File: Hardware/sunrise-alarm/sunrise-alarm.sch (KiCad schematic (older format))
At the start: 15 parts

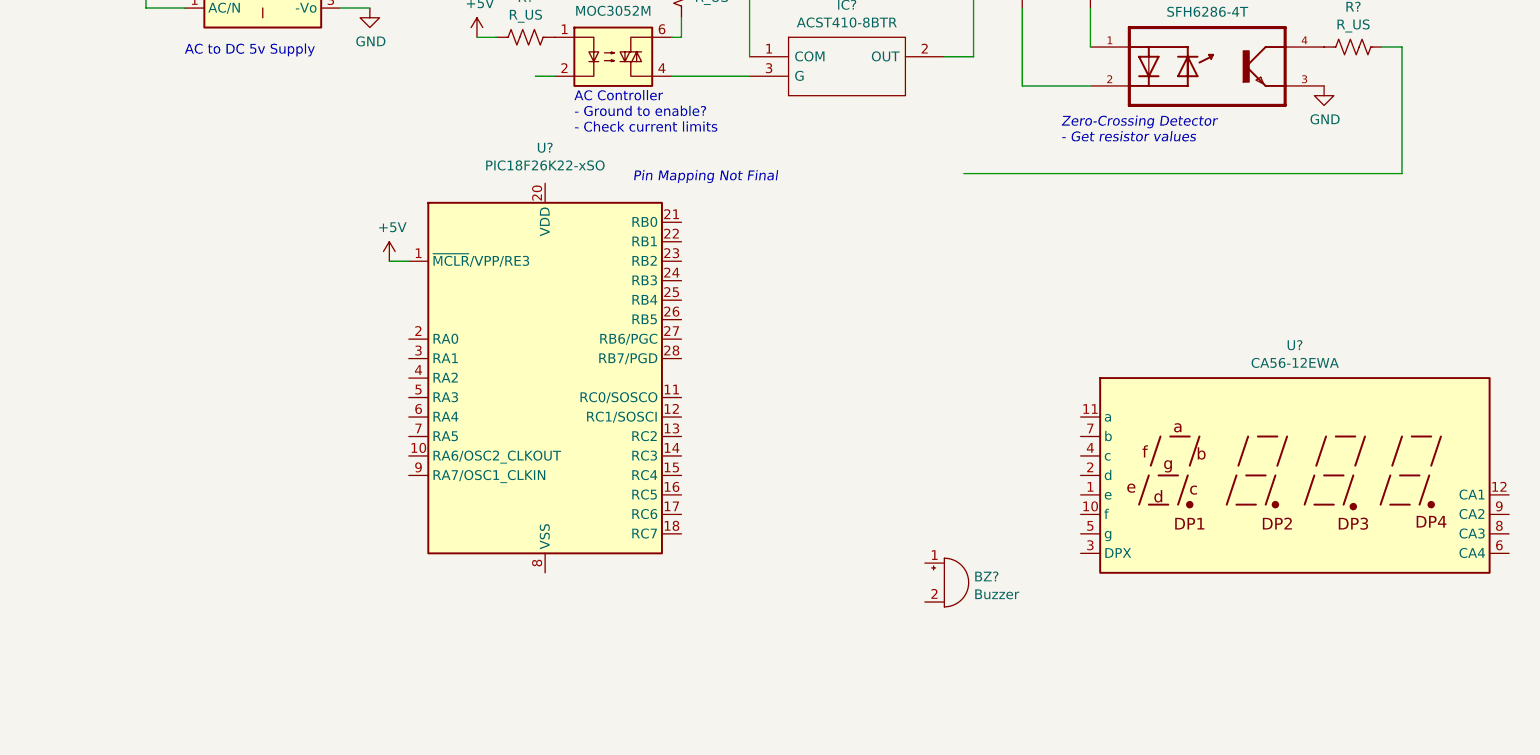
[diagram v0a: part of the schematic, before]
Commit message: Updated schematic, reset button, labeled lines
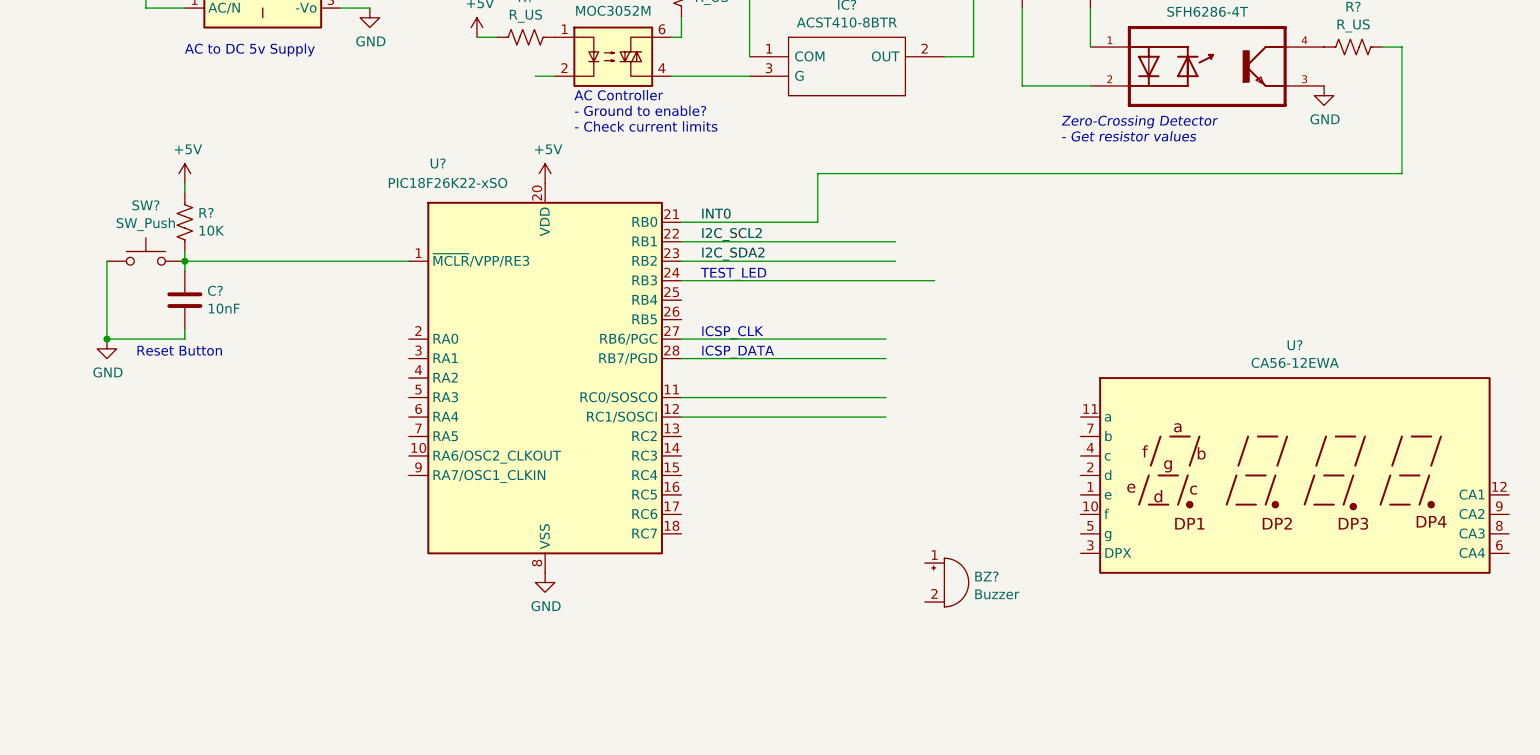
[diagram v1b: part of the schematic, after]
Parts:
- added C?: 10nF, symbol Device:C
- added R?: 10K, symbol Device:R_US
- added SW?: SW_Push, symbol Switch:SW_Push
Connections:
- net labels added: I2C_SCL2, I2C_SDA2, INT0
- wire segments 32 -> 47
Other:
- note added: "ICSP_CLK"
- note added: "ICSP_DATA"
- note added: "Reset Button"
- note added: "TEST_LED"
- note removed: "Pin Mapping Not Final"
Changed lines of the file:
@@
 $EndDescr
-$Comp
-L MCU_Microchip_PIC18:PIC18F26K22-xSO U?
-U 1 1 61792C0A
-P 3250 3450
-F 0 "U?" H 3250 4631 50  0000 C CNN
-F 1 "PIC18F26K22-xSO" H 3250 4540 50  0000 C CNN
-F 2 "Package_SO:SOIC-28W_7.5x17.9mm_P1.27mm" H 3450 3450 50  0001 C CNN
-F 3 "http://ww1.microchip.com/downloads/en/DeviceDoc/40001412G.pdf" H 3450 3450 50  0001 C CNN
-	1    3250 3450
-	1    0    0    -1
-$EndComp
 $Comp
 L Converter_ACDC:IRM-05-5 PS?
@@
 L power:+5V #PWR?
 U 1 1 617CDBCF
-P 2450 2850
-F 0 "#PWR?" H 2450 2700 50  0001 C CNN
-F 1 "+5V" H 2465 3023 50  0000 C CNN
-F 2 "" H 2450 2850 50  0001 C CNN
-F 3 "" H 2450 2850 50  0001 C CNN
-	1    2450 2850
-	1    0    0    -1
-$EndComp
-Wire Wire Line
-	2450 2850 2550 2850
+P 3250 2450
+F 0 "#PWR?" H 3250 2300 50  0001 C CNN
+F 1 "+5V" H 3265 2623 50  0000 C CNN
+F 2 "" H 3250 2450 50  0001 C CNN
+F 3 "" H 3250 2450 50  0001 C CNN
+	1    3250 2450
+	1    0    0    -1
+$EndComp
 Text Notes 8150 7650 0    50   ~ 0
 2021-10-27
@@
 Text Notes 5900 2250 0    50   Italic 0
 Zero-Crossing Detector\n- Get resistor values
-Text Notes 3700 2450 0    50   Italic 0
-Pin Mapping Not Final
 $Comp
 L Device:R_US R?
@@
 Wire Wire Line
 	7650 1750 7650 2400
-Wire Wire Line
-	7650 2400 5400 2400
+$Comp
+L power:GND #PWR?
+U 1 1 617BCF12
+P 3250 4450
+F 0 "#PWR?" H 3250 4200 50  0001 C CNN
+F 1 "GND" H 3255 4277 50  0000 C CNN
+F 2 "" H 3250 4450 50  0001 C CNN
+F 3 "" H 3250 4450 50  0001 C CNN
+	1    3250 4450
+	1    0    0    -1
+$EndComp
+Wire Wire Line
+	1400 2850 1400 2800
+$Comp
+L Device:R_US R?
+U 1 1 617BE3B8
+P 1400 2650
+F 0 "R?" H 1468 2696 50  0000 L CNN
+F 1 "10K" H 1468 2605 50  0000 L CNN
+F 2 "" V 1440 2640 50  0001 C CNN
+F 3 "~" H 1400 2650 50  0001 C CNN
+	1    1400 2650
+	1    0    0    -1
+$EndComp
+Wire Wire Line
+	1400 2500 1400 2450
+$Comp
+L power:+5V #PWR?
+U 1 1 617BF7D0
+P 1400 2450
+F 0 "#PWR?" H 1400 2300 50  0001 C CNN
+F 1 "+5V" H 1415 2623 50  0000 C CNN
+F 2 "" H 1400 2450 50  0001 C CNN
+F 3 "" H 1400 2450 50  0001 C CNN
+	1    1400 2450
+	1    0    0    -1
+$EndComp
+$Comp
+L Switch:SW_Push SW?
+U 1 1 617C3584
+P 1200 2850
+F 0 "SW?" H 1200 3135 50  0000 C CNN
+F 1 "SW_Push" H 1200 3044 50  0000 C CNN
+F 2 "" H 1200 3050 50  0001 C CNN
+F 3 "~" H 1200 3050 50  0001 C CNN
+	1    1200 2850
+	1    0    0    -1
+$EndComp
+Connection ~ 1400 2850
+$Comp
+L Device:C C?
+U 1 1 617C3D3F
+P 1400 3050
+F 0 "C?" H 1515 3096 50  0000 L CNN
+F 1 "10nF" H 1515 3005 50  0000 L CNN
+F 2 "" H 1438 2900 50  0001 C CNN
+F 3 "~" H 1400 3050 50  0001 C CNN
+	1    1400 3050
+	1    0    0    -1
+$EndComp
+Wire Wire Line
+	1400 3250 1000 3250
+Wire Wire Line
+	1000 3250 1000 2850
+$Comp
+L power:GND #PWR?
+U 1 1 617C5B85
+P 1000 3250
+F 0 "#PWR?" H 1000 3000 50  0001 C CNN
+F 1 "GND" H 1005 3077 50  0000 C CNN
+F 2 "" H 1000 3250 50  0001 C CNN
+F 3 "" H 1000 3250 50  0001 C CNN
+	1    1000 3250
+	1    0    0    -1
+$EndComp
+Connection ~ 1000 3250
+Wire Wire Line
+	1400 2900 1400 2850
+Wire Wire Line
+	1400 3250 1400 3200
+Wire Wire Line
+	1400 2850 2550 2850
+Text Notes 1150 3350 0    50   ~ 0
+Reset Button
+$Comp
+L MCU_Microchip_PIC18:PIC18F26K22-xSO U?
+U 1 1 61792C0A
+P 3250 3450
+F 0 "U?" H 2700 4550 50  0000 C CNN
+F 1 "PIC18F26K22-xSO" H 2750 4450 50  0000 C CNN
+F 2 "Package_SO:SOIC-28W_7.5x17.9mm_P1.27mm" H 3450 3450 50  0001 C CNN
+F 3 "http://ww1.microchip.com/downloads/en/DeviceDoc/40001412G.pdf" H 3450 3450 50  0001 C CNN
+	1    3250 3450
+	1    0    0    -1
+$EndComp
+Wire Wire Line
+	3950 2650 4650 2650
+Wire Wire Line
+	4650 2650 4650 2400
+Wire Wire Line
+	4650 2400 7650 2400
+Wire Wire Line
+	3950 2750 5050 2750
+Wire Wire Line
+	3950 2850 5050 2850
+Text Label 4050 2750 0    50   ~ 0
+I2C_SCL2
+Text Label 4050 2850 0    50   ~ 0
+I2C_SDA2
+Text Label 4050 2650 0    50   ~ 0
+INT0
+Wire Wire Line
+	3950 3550 5000 3550
+Wire Wire Line
+	3950 3650 5000 3650
+Wire Wire Line
+	3950 3250 5000 3250
+Wire Wire Line
+	3950 3350 5000 3350
+Text Notes 4050 3350 0    50   ~ 0
+ICSP_DATA
+Text Notes 4050 3250 0    50   ~ 0
+ICSP_CLK
+Text Notes 4050 2950 0    50   ~ 0
+TEST_LED
+Wire Wire Line
+	3950 2950 5250 2950
 $EndSCHEMATC

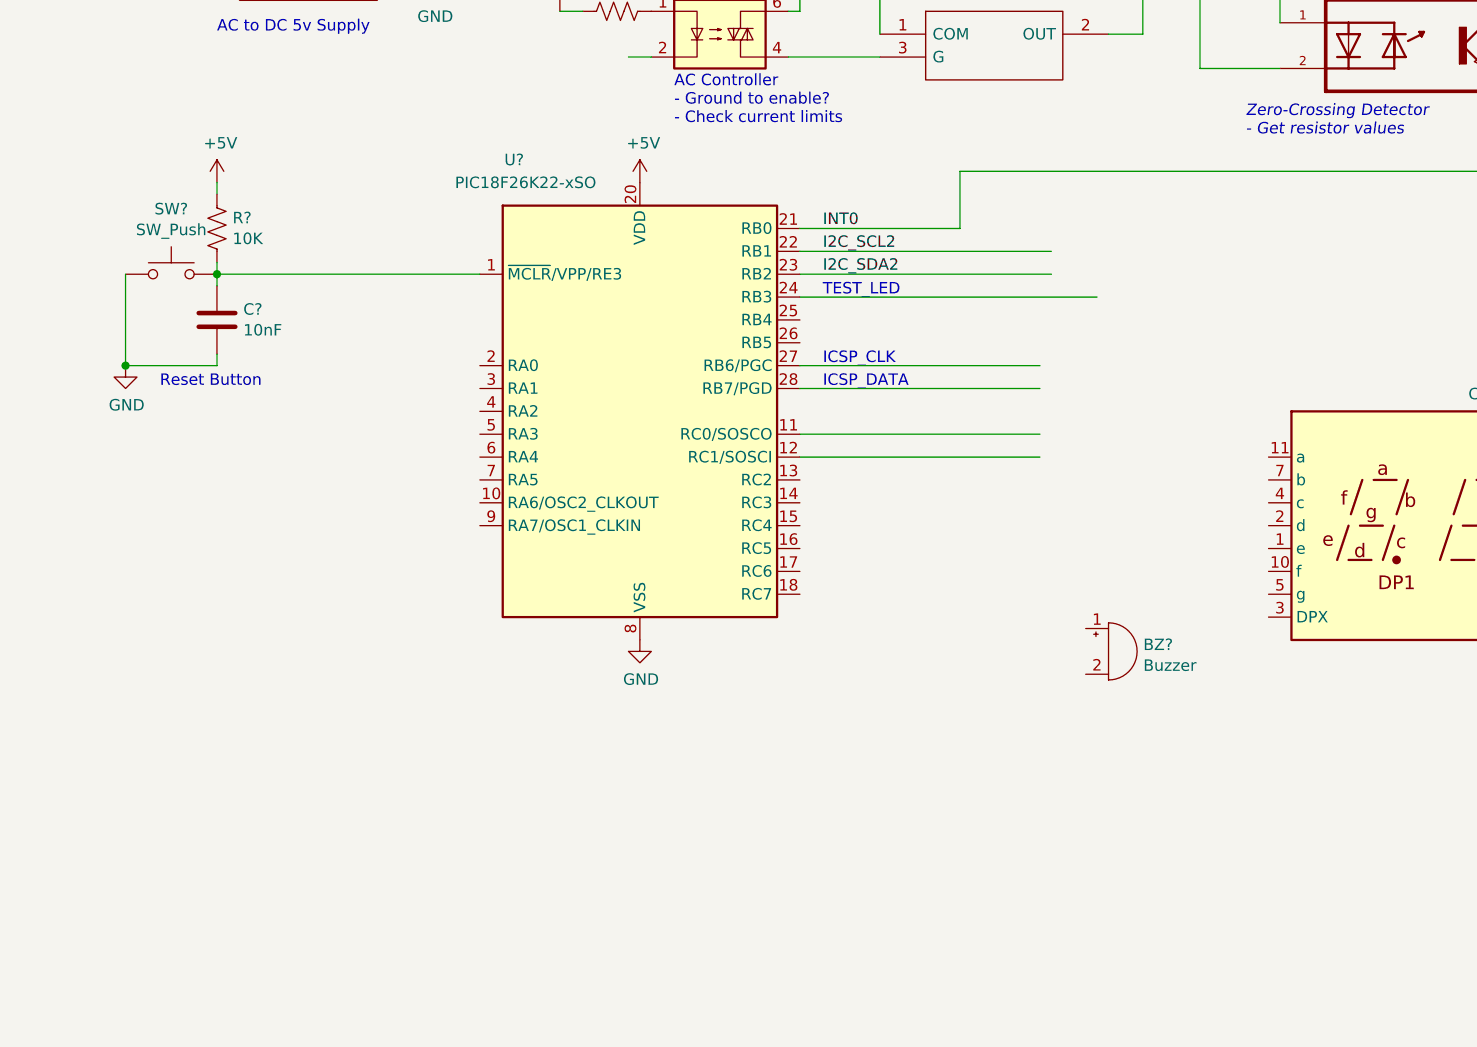
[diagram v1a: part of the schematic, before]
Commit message: Schematic: Added programing header
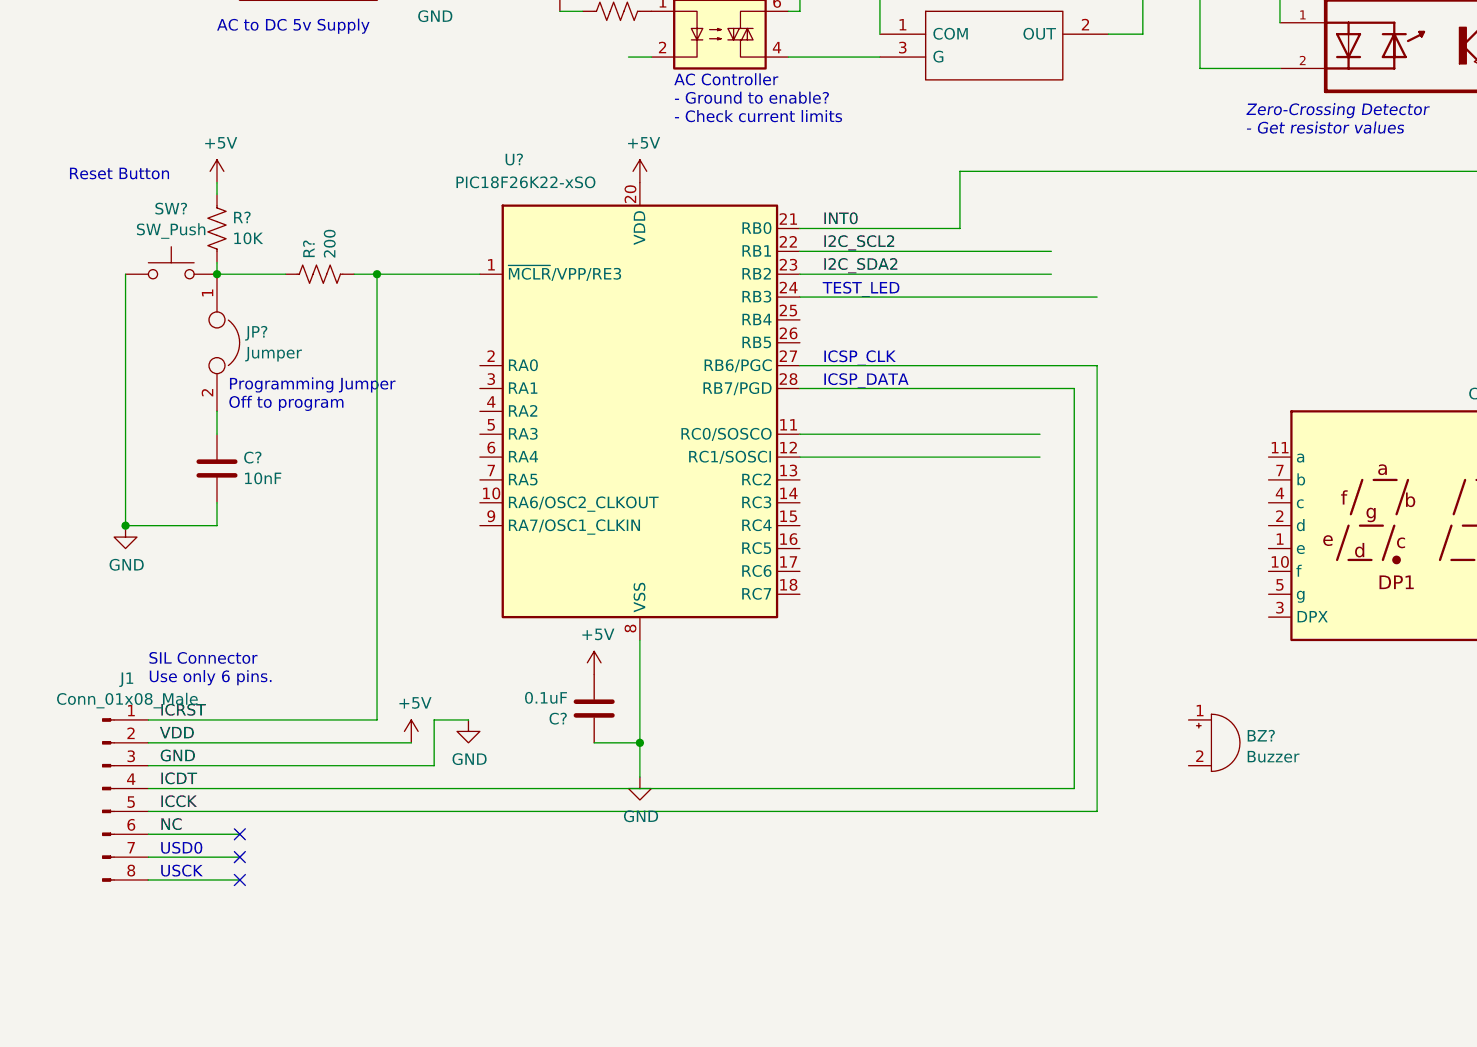
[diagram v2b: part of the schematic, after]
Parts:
- added C?: 0.1uF, symbol Device:C
- added J1: Conn_01x08_Male, symbol Connector:Conn_01x08_Male
- added JP?: Jumper, symbol Device:Jumper
- added R?: 200, symbol Device:R_US
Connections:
- net labels added: ICCK, ICDT, ICRST, NC, VDD
- wire segments 47 -> 65
- no-connect marks 0 -> 3
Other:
- note added: "Programming Jumper\nOff to program"
- note added: "SIL Connector\nUse only 6 pins."
- note added: "USCK"
- note added: "USD0"
- moved on the sheet: BZ?, C?
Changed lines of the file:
@@
 L Device:Buzzer BZ?
 U 1 1 617BFC39
-P 5300 4500
-F 0 "BZ?" H 5452 4529 50  0000 L CNN
-F 1 "Buzzer" H 5452 4438 50  0000 L CNN
-F 2 "" V 5275 4600 50  0001 C CNN
-F 3 "~" V 5275 4600 50  0001 C CNN
-	1    5300 4500
+P 5750 4900
+F 0 "BZ?" H 5902 4929 50  0000 L CNN
+F 1 "Buzzer" H 5902 4838 50  0000 L CNN
+F 2 "" V 5725 5000 50  0001 C CNN
+F 3 "~" V 5725 5000 50  0001 C CNN
+	1    5750 4900
 	1    0    0    -1
 $EndComp
@@
 Wire Wire Line
 	7650 1750 7650 2400
-$Comp
-L power:GND #PWR?
-U 1 1 617BCF12
-P 3250 4450
-F 0 "#PWR?" H 3250 4200 50  0001 C CNN
-F 1 "GND" H 3255 4277 50  0000 C CNN
-F 2 "" H 3250 4450 50  0001 C CNN
-F 3 "" H 3250 4450 50  0001 C CNN
-	1    3250 4450
-	1    0    0    -1
-$EndComp
 Wire Wire Line
 	1400 2850 1400 2800
@@
 L Device:C C?
 U 1 1 617C3D3F
-P 1400 3050
-F 0 "C?" H 1515 3096 50  0000 L CNN
-F 1 "10nF" H 1515 3005 50  0000 L CNN
-F 2 "" H 1438 2900 50  0001 C CNN
-F 3 "~" H 1400 3050 50  0001 C CNN
-	1    1400 3050
-	1    0    0    -1
-$EndComp
-Wire Wire Line
-	1400 3250 1000 3250
-Wire Wire Line
-	1000 3250 1000 2850
+P 1400 3700
+F 0 "C?" H 1515 3746 50  0000 L CNN
+F 1 "10nF" H 1515 3655 50  0000 L CNN
+F 2 "" H 1438 3550 50  0001 C CNN
+F 3 "~" H 1400 3700 50  0001 C CNN
+	1    1400 3700
+	1    0    0    -1
+$EndComp
+Wire Wire Line
+	1400 3950 1000 3950
 $Comp
 L power:GND #PWR?
 U 1 1 617C5B85
-P 1000 3250
-F 0 "#PWR?" H 1000 3000 50  0001 C CNN
-F 1 "GND" H 1005 3077 50  0000 C CNN
-F 2 "" H 1000 3250 50  0001 C CNN
-F 3 "" H 1000 3250 50  0001 C CNN
-	1    1000 3250
-	1    0    0    -1
-$EndComp
-Connection ~ 1000 3250
-Wire Wire Line
-	1400 2900 1400 2850
-Wire Wire Line
-	1400 3250 1400 3200
-Wire Wire Line
-	1400 2850 2550 2850
-Text Notes 1150 3350 0    50   ~ 0
+P 1000 3950
+F 0 "#PWR?" H 1000 3700 50  0001 C CNN
+F 1 "GND" H 1005 3777 50  0000 C CNN
+F 2 "" H 1000 3950 50  0001 C CNN
+F 3 "" H 1000 3950 50  0001 C CNN
+	1    1000 3950
+	1    0    0    -1
+$EndComp
+Connection ~ 1000 3950
+Wire Wire Line
+	1400 3950 1400 3850
+Wire Wire Line
+	1400 2850 1700 2850
+Text Notes 750  2450 0    50   ~ 0
 Reset Button
 $Comp
@@
 Wire Wire Line
 	3950 3650 5000 3650
-Wire Wire Line
-	3950 3250 5000 3250
-Wire Wire Line
-	3950 3350 5000 3350
 Text Notes 4050 3350 0    50   ~ 0
 ICSP_DATA
@@
 Wire Wire Line
 	3950 2950 5250 2950
+Wire Wire Line
+	1100 5300 1500 5300
+$Comp
+L Connector:Conn_01x08_Male J1
+U 1 1 61834A34
+P 900 5100
+F 0 "J1" H 1008 5581 50  0000 C CNN
+F 1 "Conn_01x08_Male" H 1008 5490 50  0000 C CNN
+F 2 "" H 900 5100 50  0001 C CNN
+F 3 "~" H 900 5100 50  0001 C CNN
+	1    900  5100
+	1    0    0    -1
+$EndComp
+$Comp
+L Device:C C?
+U 1 1 61839E19
+P 3050 4750
+F 0 "C?" H 3165 4796 50  0000 L CNN
+F 1 "0.1uF" H 3165 4705 50  0000 L CNN
+F 2 "" H 3088 4600 50  0001 C CNN
+F 3 "~" H 3050 4750 50  0001 C CNN
+	1    3050 4750
+	-1   0    0    1
+$EndComp
+$Comp
+L power:+5V #PWR?
+U 1 1 61845E96
+P 3050 4600
+F 0 "#PWR?" H 3050 4450 50  0001 C CNN
+F 1 "+5V" H 3065 4773 50  0000 C CNN
+F 2 "" H 3050 4600 50  0001 C CNN
+F 3 "" H 3050 4600 50  0001 C CNN
+	1    3050 4600
+	1    0    0    -1
+$EndComp
+$Comp
+L power:GND #PWR?
+U 1 1 61846300
+P 3250 5050
+F 0 "#PWR?" H 3250 4800 50  0001 C CNN
+F 1 "GND" H 3255 4877 50  0000 C CNN
+F 2 "" H 3250 5050 50  0001 C CNN
+F 3 "" H 3250 5050 50  0001 C CNN
+	1    3250 5050
+	1    0    0    -1
+$EndComp
+Wire Wire Line
+	3050 4900 3250 4900
+Wire Wire Line
+	3250 4900 3250 4450
+Connection ~ 3250 4900
+Wire Wire Line
+	3250 5050 3250 4900
+$Comp
+L Device:Jumper JP?
+U 1 1 6185279F
+P 1400 3150
+F 0 "JP?" V 1354 3277 50  0000 L CNN
+F 1 "Jumper" V 1445 3277 50  0000 L CNN
+F 2 "" H 1400 3150 50  0001 C CNN
+F 3 "~" H 1400 3150 50  0001 C CNN
+	1    1400 3150
+	0    1    1    0
+$EndComp
+Wire Wire Line
+	1000 2850 1000 3950
+Wire Wire Line
+	1400 3450 1400 3550
+Text Notes 1450 3450 0    50   ~ 0
+Programming Jumper\nOff to program
+$Comp
+L Device:R_US R?
+U 1 1 6186145D
+P 1850 2850
+F 0 "R?" H 1918 2896 50  0000 L CNN
+F 1 "200" H 1918 2805 50  0000 L CNN
+F 2 "" V 1890 2840 50  0001 C CNN
+F 3 "~" H 1850 2850 50  0001 C CNN
+	1    1850 2850
+	0    -1   -1   0
+$EndComp
+Wire Wire Line
+	2000 2850 2100 2850
+Text Notes 1100 4650 0    50   ~ 0
+SIL Connector\nUse only 6 pins.
+Text Label 1150 4800 0    50   ~ 0
+ICRST
+Text Label 1150 4900 0    50   ~ 0
+VDD
+Text Label 1150 5000 0    50   ~ 0
+GND
+Text Label 1150 5100 0    50   ~ 0
+ICDT
+Text Label 1150 5200 0    50   ~ 0
+ICCK
+Text Label 1150 5300 0    50   ~ 0
+NC
+NoConn ~ 1500 5300
+Wire Wire Line
+	1100 5400 1500 5400
+Wire Wire Line
+	1100 5500 1500 5500
+NoConn ~ 1500 5400
+NoConn ~ 1500 5500
+Text Notes 1150 5400 0    50   ~ 0
+USD0
+Text Notes 1150 5500 0    50   ~ 0
+USCK
+Wire Wire Line
+	2100 2850 2100 4800
+Wire Wire Line
+	1100 4800 2100 4800
+Connection ~ 2100 2850
+Wire Wire Line
+	2100 2850 2550 2850
+Wire Wire Line
+	1100 4900 2250 4900
+$Comp
+L power:+5V #PWR?
+U 1 1 6187BF10
+P 2250 4900
+F 0 "#PWR?" H 2250 4750 50  0001 C CNN
+F 1 "+5V" H 2265 5073 50  0000 C CNN
+F 2 "" H 2250 4900 50  0001 C CNN
+F 3 "" H 2250 4900 50  0001 C CNN
+	1    2250 4900
+	1    0    0    -1
+$EndComp
+$Comp
+L power:GND #PWR?
+U 1 1 6187C34D
+P 2500 4800
+F 0 "#PWR?" H 2500 4550 50  0001 C CNN
+F 1 "GND" H 2505 4627 50  0000 C CNN
+F 2 "" H 2500 4800 50  0001 C CNN
+F 3 "" H 2500 4800 50  0001 C CNN
+	1    2500 4800
+	1    0    0    -1
+$EndComp
+Wire Wire Line
+	1100 5000 2350 5000
+Wire Wire Line
+	5150 5100 5150 3350
+Wire Wire Line
+	3950 3350 5150 3350
+Wire Wire Line
+	1100 5100 5150 5100
+Wire Wire Line
+	5250 3250 5250 5200
+Wire Wire Line
+	3950 3250 5250 3250
+Wire Wire Line
+	1100 5200 5250 5200
+Wire Wire Line
+	2500 4800 2350 4800
+Wire Wire Line
+	2350 4800 2350 5000
 $EndSCHEMATC
